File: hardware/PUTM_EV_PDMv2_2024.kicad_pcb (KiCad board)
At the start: 4 copper layers, 58 x 87.3 mm, 159 parts, among them IC1 BTS722204ESAXUMA1, IC2 BTS722204ESAXUMA1, IC3 BTS722204ESAXUMA1, IC4 BTS722204ESAXUMA1, J1 74650073R, J4 Conn_01x06, J5 UMPT-08-01-L-RA-WT-P-TR, J6 FTSH-107-01-L-DV-K-A, J7 USB_C_Receptacle_USB2.0_14P, J8 UMPT-08-01-L-RA-WT-P-TR, U1 STM32G0C1KCTxN, U2 LD1117S33TR_SOT223, U3 LM2675M-5.0/NOPB, U4 MCP2542FDxMF

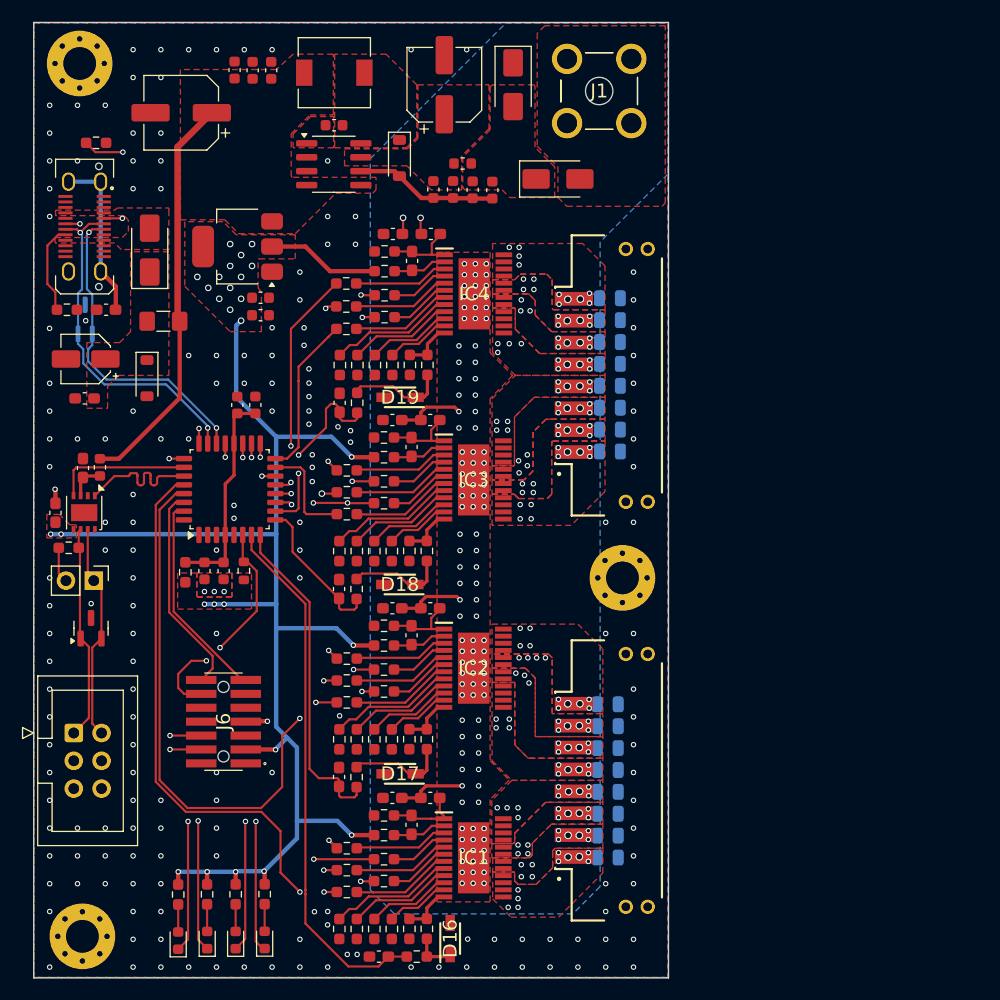
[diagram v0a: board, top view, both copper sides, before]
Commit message: cube->cmake port, current calc fix, spi datalength fix, hard-v1.1.0 sync
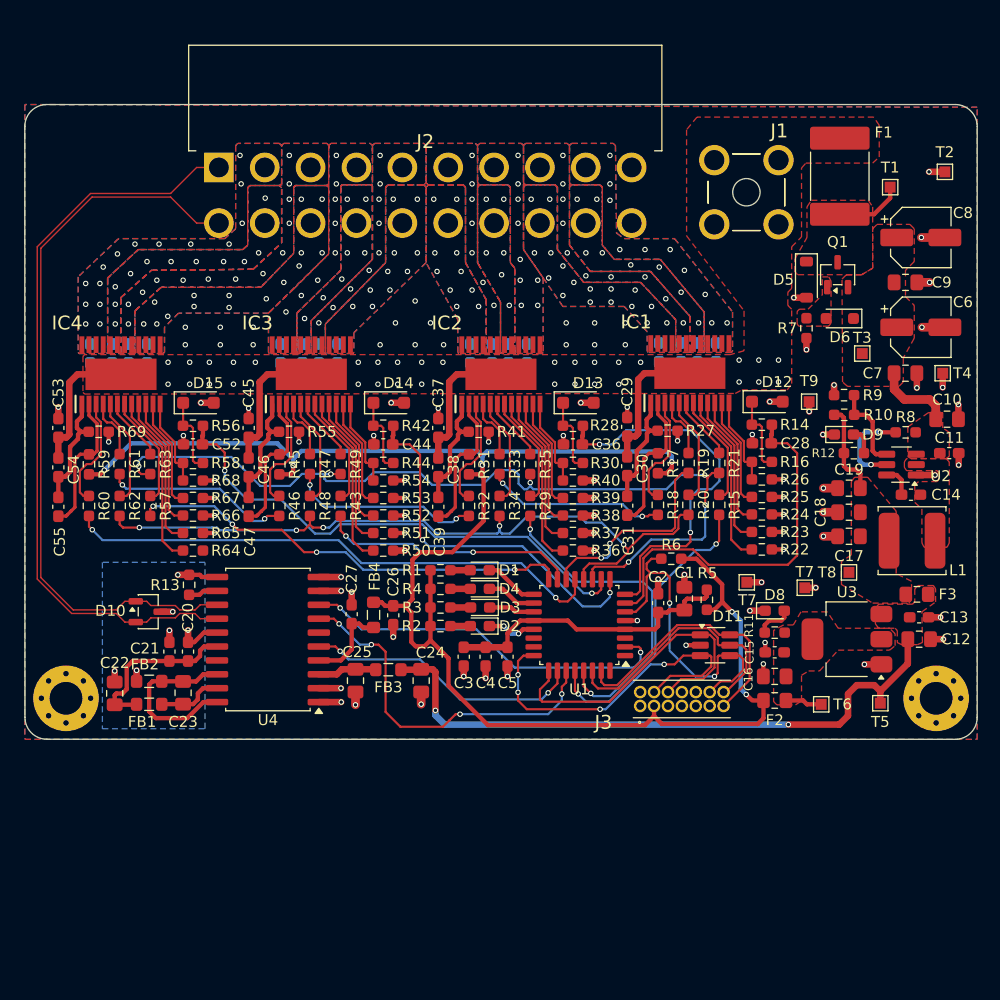
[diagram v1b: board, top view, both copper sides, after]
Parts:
- removed D16, D17, D18, D19: SKL34, SKL34:SODFL3718X140N
- removed G*** (x2): LOGO, LOGO
- removed G***: LOGO, Logos:SignatureBox25mm
- removed G***: LOGO, logos:PUTM_LOGO_15mm
- removed J4: Conn_01x06, Connector_IDC:IDC-Header_2x03_P2.54mm_Vertical
- removed J5, J8: UMPT-08-01-L-RA-WT-P-TR, UMPT-08-01-L-RA-WT-P-TR:SAMTEC_UMPT-08-01-L-RA-WT-P-TR
- removed J6: FTSH-107-01-L-DV-K-A, FTSH-107-01-L-DV-K-A:FTSH-107-XX-YYY-DV-K-A
- removed J7: USB_C_Receptacle_USB2.0_14P, Connector_USB:USB_C_Receptacle_JAE_DX07S024WJ3R400
- removed JP1: Jumper_2_Bridged, Connector_PinHeader_2.54mm:PinHeader_1x02_P2.54mm_Vertical
- removed L2: 47u, Inductor_SMD:L_6.3x6.3_H3
- removed the REF** at (174.6, 105.2)
- removed the REF** at (125.0, 58.2)
- removed the REF** at (125.2, 138.0)
- added C54: 22n, Capacitor_SMD:C_0603_1608Metric_Pad1.08x0.95mm_HandSolder, F.Cu at (123.0, 95.2)
- added C55: 470n, Capacitor_SMD:C_0603_1608Metric_Pad1.08x0.95mm_HandSolder, F.Cu at (123.0, 98.8)
- added C56: 10n, Capacitor_SMD:C_0603_1608Metric_Pad1.08x0.95mm_HandSolder, B.Cu at (126.0, 84.8)
- added C57: 10n, Capacitor_SMD:C_0603_1608Metric_Pad1.08x0.95mm_HandSolder, B.Cu at (128.0, 84.8)
- added C58: 10n, Capacitor_SMD:C_0603_1608Metric_Pad1.08x0.95mm_HandSolder, B.Cu at (129.5, 84.8)
- added C59: 10n, Capacitor_SMD:C_0603_1608Metric_Pad1.08x0.95mm_HandSolder, B.Cu at (131.2, 84.8)
- added D13: 40V/3A, Diode_SMD:D_SOD-123F, F.Cu at (170.6, 89.2)
- added D14: 40V/3A, Diode_SMD:D_SOD-123F, F.Cu at (153.2, 89.2)
- added D15: 40V/3A, Diode_SMD:D_SOD-123F, F.Cu at (135.8, 89.2)
- added F2: 6V/1A, Fuse:Fuse_0805_2012Metric_Pad1.15x1.40mm_HandSolder, F.Cu at (188.5, 116.5)
- added F3: 6V/1A, Fuse:Fuse_0805_2012Metric_Pad1.15x1.40mm_HandSolder, F.Cu at (201.5, 106.8)
- added FB1: 2K@100MHz, Inductor_SMD:L_0805_2012Metric_Pad1.05x1.20mm_HandSolder, F.Cu at (131.3, 116.8)
- added FB3: 2K@100MHz, Inductor_SMD:L_0805_2012Metric_Pad1.05x1.20mm_HandSolder, F.Cu at (153.2, 113.6)
- added FB4: 2K@100MHz, Inductor_SMD:L_0805_2012Metric_Pad1.05x1.20mm_HandSolder, F.Cu at (151.8, 108.6)
- added J2: IPBS-110-01-XX-D-GP, PDM:IPBT110H1TDRAGP, F.Cu at (137.7, 67.8)
- added J3: FTSH-107-01-L-D-K, PDM:FTSH-107-XX-YYY-D-K, F.Cu at (176.2, 117.0)
- added Q1: 30V/5A, Package_TO_SOT_SMD:SOT-23-3, F.Cu at (194.2, 77.5)
- added R66: 10k, Resistor_SMD:R_0603_1608Metric_Pad0.98x0.95mm_HandSolder, F.Cu at (135.3, 99.5)
- added R67: 10k, Resistor_SMD:R_0603_1608Metric_Pad0.98x0.95mm_HandSolder, F.Cu at (135.3, 98.0)
- added R68: 1k2, Resistor_SMD:R_0603_1608Metric_Pad0.98x0.95mm_HandSolder, F.Cu at (135.3, 96.3)
- added R69: 47R, Resistor_SMD:R_0603_1608Metric_Pad0.98x0.95mm_HandSolder, F.Cu at (126.7, 91.9)
- added REF**: MountingHole_3mm_Pad_Via, MountingHole:MountingHole_3mm_Pad_Via, F.Cu at (123.8, 116.2)
- added REF**: MountingHole_3mm_Pad_Via, MountingHole:MountingHole_3mm_Pad_Via, F.Cu at (203.2, 116.2)
- added T1: TP_VCC, TestPoint:TestPoint_Pad_1.0x1.0mm, F.Cu at (199.1, 69.5)
- added T2: TP_GND, TestPoint:TestPoint_Pad_1.0x1.0mm, F.Cu at (204.1, 68.2)
- added T3: TP_VCC, TestPoint:TestPoint_Pad_1.0x1.0mm, F.Cu at (196.5, 84.8)
- added T4: TP_GND, TestPoint:TestPoint_Pad_1.0x1.0mm, F.Cu at (203.8, 86.5)
- added T5: TP_+5V, TestPoint:TestPoint_Pad_1.0x1.0mm, F.Cu at (198.2, 116.7)
- added T6: TP_+3V3, TestPoint:TestPoint_Pad_1.0x1.0mm, F.Cu at (192.8, 116.8)
- added T7: TP_GND, TestPoint:TestPoint_Pad_1.0x1.0mm, F.Cu at (191.2, 106.2)
- added T7: TP_GND, TestPoint:TestPoint_Pad_1.0x1.0mm, F.Cu at (185.9, 105.7)
- added T8: TP_+5V, TestPoint:TestPoint_Pad_1.0x1.0mm, F.Cu at (195.3, 104.7)
- added T9: TP_GND, TestPoint:TestPoint_Pad_1.0x1.0mm, F.Cu at (191.7, 89.2)
- C1, C7: value 100n -> 10u; footprint Capacitor_SMD:C_0603_1608Metric -> Capacitor_SMD:C_0805_2012Metric_Pad1.18x1.45mm_HandSolder
- C10, C16: value 100n -> 22u; footprint Capacitor_SMD:C_0603_1608Metric -> Capacitor_SMD:C_0805_2012Metric_Pad1.18x1.45mm_HandSolder
- C11, C15, C5: value 1u -> 100n; footprint Capacitor_SMD:C_0603_1608Metric -> Capacitor_SMD:C_0603_1608Metric_Pad1.08x0.95mm_HandSolder
- C12: value 10n -> 10u; footprint Capacitor_SMD:C_0603_1608Metric -> Capacitor_SMD:C_0805_2012Metric_Pad1.18x1.45mm_HandSolder
- C13: footprint Capacitor_SMD:C_0603_1608Metric -> Capacitor_SMD:C_0603_1608Metric_Pad1.08x0.95mm_HandSolder
- C14: value 68u -> 100n; footprint Capacitor_SMD:CP_Elec_6.3x5.4 -> Capacitor_SMD:C_0603_1608Metric_Pad1.08x0.95mm_HandSolder
- C17: value 220p -> 22u; footprint Capacitor_SMD:C_0603_1608Metric_Pad1.08x0.95mm_HandSolder -> Capacitor_SMD:C_0805_2012Metric_Pad1.18x1.45mm_HandSolder
- C18: value 100n -> 22u; footprint Capacitor_SMD:C_0603_1608Metric_Pad1.08x0.95mm_HandSolder -> Capacitor_SMD:C_0805_2012Metric_Pad1.18x1.45mm_HandSolder
- C19: value 22n -> 22u; footprint Capacitor_SMD:C_0603_1608Metric_Pad1.08x0.95mm_HandSolder -> Capacitor_SMD:C_0805_2012Metric_Pad1.18x1.45mm_HandSolder
- C2: value 4.7u -> 4u7; footprint Capacitor_SMD:C_0603_1608Metric -> Capacitor_SMD:C_0603_1608Metric_Pad1.08x0.95mm_HandSolder
- C20: value 470n -> 100n
- C21: footprint Capacitor_SMD:C_0805_2012Metric -> Capacitor_SMD:C_0603_1608Metric_Pad1.08x0.95mm_HandSolder; moved to F.Cu
- C22, C23, C24: value 10n -> 47u; footprint Capacitor_SMD:C_0805_2012Metric -> Capacitor_SMD:C_0805_2012Metric_Pad1.18x1.45mm_HandSolder; moved to F.Cu
- C25: value 100n -> 47u; footprint Capacitor_SMD:C_0603_1608Metric_Pad1.08x0.95mm_HandSolder -> Capacitor_SMD:C_0805_2012Metric_Pad1.18x1.45mm_HandSolder
- C27: value 22u -> 10n; footprint Capacitor_SMD:CP_Elec_4x4.5 -> Capacitor_SMD:C_0603_1608Metric_Pad1.08x0.95mm_HandSolder
- C28: value 1u -> 220p
- C29, C37, C45: value 220p -> 100n
- C3: value 100n -> 4u7; footprint Capacitor_SMD:C_0603_1608Metric -> Capacitor_SMD:C_0603_1608Metric_Pad1.08x0.95mm_HandSolder
- C30, C38, C46: value 100n -> 22n
- C31, C39, C47: value 22n -> 470n
- C32, C40, C48: value 470n -> 10n; moved to B.Cu
- C33, C34, C35, C41, C42, C43, C49, C50, C51: footprint Capacitor_SMD:C_0805_2012Metric -> Capacitor_SMD:C_0603_1608Metric_Pad1.08x0.95mm_HandSolder
- C36, C44, C52: value 10n -> 220p; footprint Capacitor_SMD:C_0805_2012Metric -> Capacitor_SMD:C_0603_1608Metric_Pad1.08x0.95mm_HandSolder; moved to F.Cu
- C4: value 4.7u -> 100n; footprint Capacitor_SMD:C_0603_1608Metric -> Capacitor_SMD:C_0603_1608Metric_Pad1.08x0.95mm_HandSolder
- C53: value 10n -> 100n
- C6: value 10u -> 22u; footprint Capacitor_SMD:C_0603_1608Metric -> Capacitor_SMD:CP_Elec_5x5.8
- C8: value 100n -> 22u; footprint Capacitor_SMD:C_0603_1608Metric -> Capacitor_SMD:CP_Elec_5x5.8
- C9: value 100u -> 10u; footprint Capacitor_SMD:CP_Elec_6.3x7.7 -> Capacitor_SMD:C_0805_2012Metric_Pad1.18x1.45mm_HandSolder
- D1, D2, D3, D4: value 150060SS75000 -> LED_Debug; footprint LED_SMD:LED_0603_1608Metric -> LED_SMD:LED_0603_1608Metric_Pad1.05x0.95mm_HandSolder
- D10: value 0.1/1A -> PESD5V0L2BT,215; footprint Diode_SMD:D_SMA -> Package_TO_SOT_SMD:SOT-23-3
- D11: value 6V -> SP0505BAHTG; footprint Diode_SMD:D_SOD-123 -> Package_TO_SOT_SMD:SOT-23-6_Handsoldering
- D12: value TPD2E2U06QDCKRQ1 -> 40V/3A; footprint Package_TO_SOT_SMD:SOT-323_SC-70_Handsoldering -> Diode_SMD:D_SOD-123F; moved to F.Cu
- D5: value SMAJ24CA-13-F -> 30V/200W; footprint Diode_SMD:D_SMA -> Diode_SMD:D_SOD-123
- D6: value SS26FL -> 9V1/200mW; footprint Diode_SMD:D_SOD-123 -> Diode_SMD:D_SOD-323_HandSoldering
- D8: value SS34ALH -> LED_+3V3; footprint Diode_SMD:D_SMA -> LED_SMD:LED_0603_1608Metric_Pad1.05x0.95mm_HandSolder
- D9: value PESD2CAN.215 -> LED_+5V; footprint Package_TO_SOT_SMD:SOT-23 -> LED_SMD:LED_0603_1608Metric_Pad1.05x0.95mm_HandSolder
- F1: value 5V/0.5A -> 33V/1A5; footprint Fuse:Fuse_1206_3216Metric_Pad1.42x1.75mm_HandSolder -> Fuse:Fuse_2920_7451Metric_Pad2.10x5.45mm_HandSolder
- FB2: value 60R@100MHz -> 2K@100MHz; footprint Inductor_SMD:L_0603_1608Metric -> Inductor_SMD:L_0805_2012Metric_Pad1.05x1.20mm_HandSolder
- IC1, IC2, IC3, IC4: footprint BTS722204ESAXUMA1:SOP65P600X115-25N -> PDM:SOP65P600X115-25N
- J1: footprint Redcube conn:74650073R -> PDM:74650073R
- L1: value 300n -> 68u/1A4; footprint Inductor_SMD:L_0603_1608Metric -> Inductor_SMD:L_TDK_VLS6045EX_VLS6045AF
- R1, R2, R3, R4: value 150 -> 150R
- R10: value 10k -> 100k
- R11, R12: value 10k -> 1k
- R13: value 1.2k -> 100k
- R14: value 47 -> 4k7
- R15, R16: value 330 -> 4k7
- R17: value 330 -> 470R
- R18, R34, R35, R48, R49, R62, R63: value 330 -> 330R
- R19: value 100k -> 330R; footprint Resistor_SMD:R_0603_1608Metric -> Resistor_SMD:R_0603_1608Metric_Pad0.98x0.95mm_HandSolder
- R20: value 0 -> 330R
- R21: value 120 -> 330R
- R22, R23: value 5.1k -> 10k
- R24, R25, R38, R39, R52, R53: value 4.7k -> 10k
- R26, R40, R54: value 470 -> 1k2
- R27, R41, R55: value 4.7k -> 47R
- R28, R29, R30, R42, R43, R44, R56, R57, R58: value 10k -> 4k7
- R31, R45, R59: value 10k -> 470R
- R32, R46, R60: value 1.2k -> 330R
- R33, R47, R61: value 47 -> 330R
- R36, R37, R50, R51, R64, R65: value 330 -> 10k
- R5: value 4.7k -> 0
- R6: value 4.7k -> 100k
- R7: value 470 -> 100k
- R8: value 4.7k -> 510k
- R9: value 10k -> 13k3
- U2: value LD1117S33TR_SOT223 -> TPS54202HDDCR; footprint Package_TO_SOT_SMD:SOT-223-3_TabPin2 -> Package_TO_SOT_SMD:SOT-23-6_Handsoldering
- U3: value LM2675M-5.0/NOPB -> LM1117-3.3; footprint Package_SO:SOIC-8_3.9x4.9mm_P1.27mm -> Package_TO_SOT_SMD:SOT-223-3_TabPin2
- U4: value MCP2542FDxMF -> ADM3057ExRW; footprint Package_DFN_QFN:DFN-8-1EP_3x3mm_P0.65mm_EP1.55x2.4mm -> Package_SO:SOIC-20W_7.5x12.8mm_P1.27mm
- moved C14 75.3 mm to (200.9, 97.7), turned to 0 degrees
- moved C16 74.2 mm to (188.5, 114.2), turned to 180 degrees
- moved R22 71.3 mm to (187.3, 102.6)
- moved C12 71.2 mm to (201.7, 110.8)
- moved D9 71.0 mm to (194.8, 92.2), turned to 0 degrees
- moved C10 71.0 mm to (204.2, 90.8), turned to 0 degrees
- moved C15 70.3 mm to (188.5, 112.0), turned to 180 degrees
- moved R9 67.1 mm to (194.8, 88.5), turned to 0 degrees
- moved R23 66.7 mm to (187.3, 101.0)
- moved C13 66.2 mm to (201.7, 108.8)
- moved R10 64.7 mm to (194.8, 90.3), turned to 180 degrees
- moved C11 64.5 mm to (204.4, 93.8), turned to 180 degrees
- moved U3 63.9 mm to (195.1, 110.8), turned to 180 degrees
- moved U2 63.9 mm to (200.1, 94.9)
- moved F1 63.2 mm to (194.4, 68.5), turned to 90 degrees
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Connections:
- C1 pad 1: /STM_VCC -> /MCU/STM_VCC
- C10 pad 1: +5V -> +24V
- C11 pad 1: +3.3V -> GND
- C11 pad 2: GND -> +24V
- C12 pad 1: /Power/CB -> +5V
- C12 pad 2: /Power/SW_L -> GND
- C13 pad 1: +3.3V -> +5V
- C14 pad 1: +5V -> /Power/BOOT_+5V
- C14 pad 2: GND -> /Power/SW_+5V
- C15 pad 1: +5V -> /Power/VO_+3.3V
- C16 pad 1: +5V -> /Power/VO_+3.3V
- C17 pad 1: /FUSE1_IS -> /Power/+5V_OUT
- C18 pad 1: +BATT -> /Power/+5V_OUT
- C19 pad 1: +BATT -> /Power/+5V_OUT
- C19 pad 2: Net-(IC1-GND_1) -> GND
- C2 pad 1: /STM_VCC -> /MCU/STM_VCC
- C20 pad 1: Net-(IC1-GND_1) -> /CAN/CAN_GND_ISO
- C20 pad 2: Net-(IC1-VDD) -> /CAN/VISOIN
- C21 pad 1: OUT1_0 -> /CAN/VISOIN
- C21 pad 2: GND -> /CAN/CAN_GND_ISO
- C22 pad 1: OUT1_1 -> /CAN/CAN_GND_ISO
- C22 pad 2: GND -> /CAN/VISOIN
- C23 pad 1: OUT1_2 -> /CAN/GNDISO
- C23 pad 2: GND -> /CAN/VISOOUT
- C24 pad 1: OUT1_3 -> GND
- C24 pad 2: GND -> +5V
- C25 pad 1: +3.3V -> /CAN/VCC
- C26 pad 1: Net-(U4-VDD) -> +3V3
- C27 pad 1: Net-(D10-K) -> /CAN/VIO
- C28 pad 1: Net-(D10-K) -> /MCU/FUSE_IS0
- C29 pad 1: /FUSE2_IS -> +BATT
- C3 pad 1: /STM_VCC -> /MCU/STM_VCC
- C30 pad 2: GND -> /Power controllers/IC_0/PC0_GND
- C31 pad 1: +BATT -> /Power controllers/IC_0/PC0_GND
- C31 pad 2: Net-(IC2-GND_1) -> /Power controllers/IC_0/VDD
- C32 pad 1: Net-(IC2-GND_1) -> OUT0_0
- C32 pad 2: Net-(IC2-VDD) -> GND
- C33 pad 1: OUT2_0 -> OUT0_1
- C34 pad 1: OUT2_1 -> OUT0_2
- C35 pad 1: OUT2_2 -> OUT0_3
- C36 pad 1: OUT2_3 -> /MCU/FUSE_IS1
- C37 pad 1: /FUSE3_IS -> +BATT
- C38 pad 2: GND -> /Power controllers/IC_1/PC1_GND
- C39 pad 1: +BATT -> /Power controllers/IC_1/PC1_GND
- C39 pad 2: Net-(IC3-GND_1) -> /Power controllers/IC_1/VDD
- C4 pad 1: /STM_VCC -> /MCU/STM_VCC
- C40 pad 1: Net-(IC3-GND_1) -> OUT1_0
- C40 pad 2: Net-(IC3-VDD) -> GND
- C41 pad 1: OUT3_0 -> OUT1_1
- C42 pad 1: OUT3_1 -> OUT1_2
- C43 pad 1: OUT3_2 -> OUT1_3
- C44 pad 1: OUT3_3 -> /MCU/FUSE_IS2
- C45 pad 1: /FUSE4_IS -> +BATT
- C46 pad 2: GND -> /Power controllers/IC_2/PC2_GND
- C47 pad 1: +BATT -> /Power controllers/IC_2/PC2_GND
- C47 pad 2: Net-(IC4-GND_1) -> /Power controllers/IC_2/VDD
- C48 pad 1: Net-(IC4-GND_1) -> OUT2_0
- C48 pad 2: Net-(IC4-VDD) -> GND
- C49 pad 1: OUT4_0 -> OUT2_1
- C5 pad 1: GND -> /MCU/STM_VCC
- C5 pad 2: /Power/VIN_L -> GND
- C50 pad 1: OUT4_1 -> OUT2_2
- C51 pad 1: OUT4_2 -> OUT2_3
- C52 pad 1: OUT4_3 -> /MCU/FUSE_IS3
- C53 pad 1: Net-(J7-SHIELD) -> +BATT
- C6 pad 1: GND -> +24V
- C6 pad 2: /Power/VIN_L -> GND
- C7 pad 1: GND -> +24V
- C7 pad 2: /Power/VIN_SW_REG -> GND
- C8 pad 1: GND -> +24V
- C8 pad 2: /Power/VIN_SW_REG -> GND
- C9 pad 1: /Power/VIN_SW_REG -> +24V
- D1 pad 1: /LED1 -> /MCU/LED3
- D1 pad 2: Net-(D1-A) -> /MCU/LD_3_R
- D10 pad 1: Net-(D10-K) -> /CAN/CAN.N
- D10 pad 2: VBUS -> /CAN/CAN.P
- D11 pad 1: Net-(D10-K) -> /Connectors/SW.CLK
- D12 pad 1: /D- -> /Power controllers/IC_0/R_IS_PROT
- D12 pad 2: /D+ -> GND
- D2 pad 1: /LED2 -> /MCU/LED2
- D2 pad 2: Net-(D2-A) -> /MCU/LD_2_R
- D3 pad 1: /LED3 -> /MCU/LED1
- D3 pad 2: Net-(D3-A) -> /MCU/LD_1_R
- D4 pad 1: /LED4 -> /MCU/LED0
- D4 pad 2: Net-(D4-A) -> /MCU/LD_0_R
- D5 pad 1: GND -> /Power/RPP_D
- D5 pad 2: /Power/VIN_L -> GND
- D6 pad 1: /Power/SW_L -> +24V
- D6 pad 2: GND -> /Power/RPP_G
- D8 pad 1: /Power/VIN_L -> GND
- D8 pad 2: +BATT -> /Power/D3V3_R1k
- D9 pad 1: CAN_L -> GND
- D9 pad 2: CAN_H -> /Power/D5V_R1k
- F1 pad 1: +5V -> /Power/RPP_D
- F1 pad 2: Net-(D10-K) -> +BATT
- FB2 pad 1: +5V -> /CAN/GNDISO
- FB2 pad 2: Net-(U4-VDD) -> /CAN/CAN_GND_ISO
- IC1 pad 1: Net-(IC1-GND_1) -> /Power controllers/IC_0/PC0_GND
- IC1 pad 10: /Controllers/IC_1/IN2 -> /Power controllers/IC_0/IN2
- IC1 pad 11: /Controllers/IC_1/IN3 -> /Power controllers/IC_0/IN3
- IC1 pad 12: Net-(IC1-IS) -> /Power controllers/IC_0/IS
- IC1 pad 13: OUT1_3 -> OUT0_3
- IC1 pad 14: OUT1_3 -> OUT0_3
- IC1 pad 15: OUT1_3 -> OUT0_3
- IC1 pad 16: OUT1_3 -> OUT0_3
- IC1 pad 17: OUT1_2 -> OUT0_2
- IC1 pad 18: OUT1_2 -> OUT0_2
- IC1 pad 19: OUT1_1 -> OUT0_1
- IC1 pad 2: Net-(IC1-VDD) -> /Power controllers/IC_0/VDD
- IC1 pad 20: OUT1_1 -> OUT0_1
- IC1 pad 21: OUT1_0 -> OUT0_0
- IC1 pad 22: OUT1_0 -> OUT0_0
- IC1 pad 23: OUT1_0 -> OUT0_0
- IC1 pad 24: OUT1_0 -> OUT0_0
- IC1 pad 3: Net-(IC1-SO) -> /Power controllers/IC_0/SO
- IC1 pad 4: Net-(IC1-SI) -> /Power controllers/IC_0/SI
- IC1 pad 5: Net-(IC1-SCLK) -> /Power controllers/IC_0/SCLK
- IC1 pad 6: Net-(IC1-CSN) -> /Power controllers/IC_0/CSN
- IC1 pad 7: Net-(IC1-LHI) -> /Power controllers/IC_0/LHI
- IC1 pad 8: /Controllers/IC_1/IN0 -> /Power controllers/IC_0/IN0
- IC1 pad 9: /Controllers/IC_1/IN1 -> /Power controllers/IC_0/IN1
- IC2 pad 1: Net-(IC2-GND_1) -> /Power controllers/IC_1/PC1_GND
- IC2 pad 10: /Controllers/IC_2/IN2 -> /Power controllers/IC_1/IN2
- IC2 pad 11: /Controllers/IC_2/IN3 -> /Power controllers/IC_1/IN3
- IC2 pad 12: Net-(IC2-IS) -> /Power controllers/IC_1/IS
- IC2 pad 13: OUT2_3 -> OUT1_3
- IC2 pad 14: OUT2_3 -> OUT1_3
- IC2 pad 15: OUT2_3 -> OUT1_3
- IC2 pad 16: OUT2_3 -> OUT1_3
- IC2 pad 17: OUT2_2 -> OUT1_2
- IC2 pad 18: OUT2_2 -> OUT1_2
- IC2 pad 19: OUT2_1 -> OUT1_1
- IC2 pad 2: Net-(IC2-VDD) -> /Power controllers/IC_1/VDD
- IC2 pad 20: OUT2_1 -> OUT1_1
- IC2 pad 21: OUT2_0 -> OUT1_0
- IC2 pad 22: OUT2_0 -> OUT1_0
- IC2 pad 23: OUT2_0 -> OUT1_0
- IC2 pad 24: OUT2_0 -> OUT1_0
- IC2 pad 3: Net-(IC2-SO) -> /Power controllers/IC_1/SO
- IC2 pad 4: Net-(IC2-SI) -> /Power controllers/IC_1/SI
- IC2 pad 5: Net-(IC2-SCLK) -> /Power controllers/IC_1/SCLK
- IC2 pad 6: Net-(IC2-CSN) -> /Power controllers/IC_1/CSN
- IC2 pad 7: Net-(IC2-LHI) -> /Power controllers/IC_1/LHI
- IC2 pad 8: /Controllers/IC_2/IN0 -> /Power controllers/IC_1/IN0
- IC2 pad 9: /Controllers/IC_2/IN1 -> /Power controllers/IC_1/IN1
- IC3 pad 1: Net-(IC3-GND_1) -> /Power controllers/IC_2/PC2_GND
- IC3 pad 10: /Controllers/IC_3/IN2 -> /Power controllers/IC_2/IN2
- IC3 pad 11: /Controllers/IC_3/IN3 -> /Power controllers/IC_2/IN3
- IC3 pad 12: Net-(IC3-IS) -> /Power controllers/IC_2/IS
- IC3 pad 13: OUT3_3 -> OUT2_3
- IC3 pad 14: OUT3_3 -> OUT2_3
- IC3 pad 15: OUT3_3 -> OUT2_3
- IC3 pad 16: OUT3_3 -> OUT2_3
- IC3 pad 17: OUT3_2 -> OUT2_2
- IC3 pad 18: OUT3_2 -> OUT2_2
- IC3 pad 19: OUT3_1 -> OUT2_1
- IC3 pad 2: Net-(IC3-VDD) -> /Power controllers/IC_2/VDD
- IC3 pad 20: OUT3_1 -> OUT2_1
- IC3 pad 21: OUT3_0 -> OUT2_0
- IC3 pad 22: OUT3_0 -> OUT2_0
- IC3 pad 23: OUT3_0 -> OUT2_0
- IC3 pad 24: OUT3_0 -> OUT2_0
- IC3 pad 3: Net-(IC3-SO) -> /Power controllers/IC_2/SO
- IC3 pad 4: Net-(IC3-SI) -> /Power controllers/IC_2/SI
- IC3 pad 5: Net-(IC3-SCLK) -> /Power controllers/IC_2/SCLK
- IC3 pad 6: Net-(IC3-CSN) -> /Power controllers/IC_2/CSN
- IC3 pad 7: Net-(IC3-LHI) -> /Power controllers/IC_2/LHI
- IC3 pad 8: /Controllers/IC_3/IN0 -> /Power controllers/IC_2/IN0
- IC3 pad 9: /Controllers/IC_3/IN1 -> /Power controllers/IC_2/IN1
- IC4 pad 1: Net-(IC4-GND_1) -> /Power controllers/IC_3/PC3_GND
- IC4 pad 10: /Controllers/IC_4/IN2 -> /Power controllers/IC_3/IN2
- IC4 pad 11: /Controllers/IC_4/IN3 -> /Power controllers/IC_3/IN3
- IC4 pad 12: Net-(IC4-IS) -> /Power controllers/IC_3/IS
- IC4 pad 13: OUT4_3 -> OUT3_3
- IC4 pad 14: OUT4_3 -> OUT3_3
- IC4 pad 15: OUT4_3 -> OUT3_3
- IC4 pad 16: OUT4_3 -> OUT3_3
- IC4 pad 17: OUT4_2 -> OUT3_2
- IC4 pad 18: OUT4_2 -> OUT3_2
- IC4 pad 19: OUT4_1 -> OUT3_1
- IC4 pad 2: Net-(IC4-VDD) -> /Power controllers/IC_3/VDD
- IC4 pad 20: OUT4_1 -> OUT3_1
- IC4 pad 21: OUT4_0 -> OUT3_0
- IC4 pad 22: OUT4_0 -> OUT3_0
- IC4 pad 23: OUT4_0 -> OUT3_0
- IC4 pad 24: OUT4_0 -> OUT3_0
- IC4 pad 3: Net-(IC4-SO) -> /Power controllers/IC_3/SO
- IC4 pad 4: Net-(IC4-SI) -> /Power controllers/IC_3/SI
- IC4 pad 5: Net-(IC4-SCLK) -> /Power controllers/IC_3/SCLK
- IC4 pad 6: Net-(IC4-CSN) -> /Power controllers/IC_3/CSN
- IC4 pad 7: Net-(IC4-LHI) -> /Power controllers/IC_3/LHI
- IC4 pad 8: /Controllers/IC_4/IN0 -> /Power controllers/IC_3/IN0
- IC4 pad 9: /Controllers/IC_4/IN1 -> /Power controllers/IC_3/IN1
- L1 pad 1: /Power/VIN_L -> /Power/SW_+5V
- L1 pad 2: /Power/VIN_SW_REG -> /Power/+5V_OUT
- R1 pad 1: +3.3V -> /MCU/LD_3_R
- R1 pad 2: Net-(D3-A) -> +3V3
- R10 pad 1: GND -> /Power/FB_+5V
- R10 pad 2: /Controllers/IC_1/IN1 -> /Power/+5V_OUT
- R11 pad 1: GND -> /Power/VO_+3.3V
- R11 pad 2: /Controllers/IC_1/IN2 -> /Power/D3V3_R1k
- R12 pad 1: GND -> /Power/+5V_OUT
- R12 pad 2: /Controllers/IC_1/IN3 -> /Power/D5V_R1k
- R13 pad 1: Net-(IC1-IS) -> /CAN/CAN_GND_ISO
- R13 pad 2: GND -> /CAN/RS
- R14 pad 1: GND -> /MCU/FUSE_IS0
- R14 pad 2: Net-(IC1-GND_1) -> /Power controllers/IC_0/R_IS_PROT
- R15 pad 1: /Controllers/MISO_1 -> /MCU/LHI0
- R15 pad 2: Net-(IC1-SO) -> /Power controllers/IC_0/LHI
- R16 pad 1: /SPI1_MOSI -> /Power controllers/IC_0/R_IS_PROT
- R16 pad 2: Net-(IC1-SI) -> /Power controllers/IC_0/IS
- R17 pad 1: /SPI1_SCK -> +3V3
- R17 pad 2: Net-(IC1-SCLK) -> /Power controllers/IC_0/VDD
- R18 pad 1: /SPI1_NSS -> /Power controllers/IC_0/MISO
- R18 pad 2: Net-(IC1-CSN) -> /Power controllers/IC_0/SO
- R19 pad 1: +3.3V -> /MCU/SPI.MOSI
- R19 pad 2: /NRST -> /Power controllers/IC_0/SI
- R2 pad 1: +3.3V -> /MCU/LD_2_R
- R2 pad 2: Net-(D2-A) -> +3V3
- R20 pad 1: +3.3V -> /MCU/SPI.SCK
- R20 pad 2: /STM_VCC -> /Power controllers/IC_0/SCLK
- R21 pad 1: Net-(JP1-B) -> /MCU/SPI.NSS
- R21 pad 2: CAN_L -> /Power controllers/IC_0/CSN
- R22 pad 2: Net-(J7-CC1) -> /Power controllers/IC_0/IN0
- R23 pad 2: Net-(J7-CC2) -> /Power controllers/IC_0/IN1
- R24 pad 1: /FUSE2_IS -> GND
- R24 pad 2: Net-(D17-K) -> /Power controllers/IC_0/IN2
- R25 pad 1: /LHI_2 -> GND
- R25 pad 2: Net-(IC2-LHI) -> /Power controllers/IC_0/IN3
- R26 pad 1: +3.3V -> /Power controllers/IC_0/IS
- R26 pad 2: Net-(IC2-VDD) -> GND
- R27 pad 1: Net-(D17-K) -> GND
- R27 pad 2: Net-(IC2-IS) -> /Power controllers/IC_0/PC0_GND
- R28 pad 1: GND -> /MCU/FUSE_IS1
- R28 pad 2: /Controllers/IC_2/IN0 -> /Power controllers/IC_1/R_IS_PROT
- R29 pad 1: GND -> /MCU/LHI1
- R29 pad 2: /Controllers/IC_2/IN1 -> /Power controllers/IC_1/LHI
- R3 pad 1: +3.3V -> /MCU/LD_1_R
- R3 pad 2: Net-(D1-A) -> +3V3
- R30 pad 1: GND -> /Power controllers/IC_1/R_IS_PROT
- R30 pad 2: /Controllers/IC_2/IN2 -> /Power controllers/IC_1/IS
- R31 pad 1: GND -> +3V3
- R31 pad 2: /Controllers/IC_2/IN3 -> /Power controllers/IC_1/VDD
- R32 pad 1: Net-(IC2-IS) -> /Power controllers/IC_1/MISO
- R32 pad 2: GND -> /Power controllers/IC_1/SO
- R33 pad 1: GND -> /Power controllers/IC_0/MISO
- R33 pad 2: Net-(IC2-GND_1) -> /Power controllers/IC_1/SI
- R34 pad 1: /Controllers/MISO_2 -> /MCU/SPI.SCK
- R34 pad 2: Net-(IC2-SO) -> /Power controllers/IC_1/SCLK
- R35 pad 1: /Controllers/MISO_1 -> /MCU/SPI.NSS
- R35 pad 2: Net-(IC2-SI) -> /Power controllers/IC_1/CSN
- R36 pad 1: /SPI1_SCK -> GND
- R36 pad 2: Net-(IC2-SCLK) -> /Power controllers/IC_1/IN0
- R37 pad 1: /SPI1_NSS -> GND
- R37 pad 2: Net-(IC2-CSN) -> /Power controllers/IC_1/IN1
- R38 pad 1: /FUSE3_IS -> GND
- R38 pad 2: Net-(D18-K) -> /Power controllers/IC_1/IN2
- R39 pad 1: /LHI_3 -> GND
- R39 pad 2: Net-(IC3-LHI) -> /Power controllers/IC_1/IN3
- R4 pad 1: +3.3V -> /MCU/LD_0_R
- R4 pad 2: Net-(D4-A) -> +3V3
- R40 pad 1: +3.3V -> /Power controllers/IC_1/IS
- R40 pad 2: Net-(IC3-VDD) -> GND
- R41 pad 1: Net-(D18-K) -> GND
- R41 pad 2: Net-(IC3-IS) -> /Power controllers/IC_1/PC1_GND
- R42 pad 1: GND -> /MCU/FUSE_IS2
- R42 pad 2: /Controllers/IC_3/IN0 -> /Power controllers/IC_2/R_IS_PROT
- R43 pad 1: GND -> /MCU/LHI2
- R43 pad 2: /Controllers/IC_3/IN1 -> /Power controllers/IC_2/LHI
- R44 pad 1: GND -> /Power controllers/IC_2/R_IS_PROT
- R44 pad 2: /Controllers/IC_3/IN2 -> /Power controllers/IC_2/IS
- R45 pad 1: GND -> +3V3
- R45 pad 2: /Controllers/IC_3/IN3 -> /Power controllers/IC_2/VDD
- R46 pad 1: Net-(IC3-IS) -> /Power controllers/IC_2/MISO
- R46 pad 2: GND -> /Power controllers/IC_2/SO
- R47 pad 1: GND -> /Power controllers/IC_1/MISO
- R47 pad 2: Net-(IC3-GND_1) -> /Power controllers/IC_2/SI
- R48 pad 1: /Controllers/MISO_3 -> /MCU/SPI.SCK
- R48 pad 2: Net-(IC3-SO) -> /Power controllers/IC_2/SCLK
- R49 pad 1: /Controllers/MISO_2 -> /MCU/SPI.NSS
- R49 pad 2: Net-(IC3-SI) -> /Power controllers/IC_2/CSN
- R5 pad 1: /FUSE1_IS -> +3V3
- R5 pad 2: Net-(D16-K) -> /MCU/STM_VCC
- R50 pad 1: /SPI1_SCK -> GND
- R50 pad 2: Net-(IC3-SCLK) -> /Power controllers/IC_2/IN0
- R51 pad 1: /SPI1_NSS -> GND
- R51 pad 2: Net-(IC3-CSN) -> /Power controllers/IC_2/IN1
- R52 pad 1: /FUSE4_IS -> GND
- R52 pad 2: Net-(D19-K) -> /Power controllers/IC_2/IN2
- R53 pad 1: /LHI_4 -> GND
- R53 pad 2: Net-(IC4-LHI) -> /Power controllers/IC_2/IN3
- R54 pad 1: +3.3V -> /Power controllers/IC_2/IS
- R54 pad 2: Net-(IC4-VDD) -> GND
- R55 pad 1: Net-(D19-K) -> GND
- R55 pad 2: Net-(IC4-IS) -> /Power controllers/IC_2/PC2_GND
- R56 pad 1: GND -> /MCU/FUSE_IS3
- R56 pad 2: /Controllers/IC_4/IN0 -> /Power controllers/IC_3/R_IS_PROT
- R57 pad 1: GND -> /MCU/LHI3
- R57 pad 2: /Controllers/IC_4/IN1 -> /Power controllers/IC_3/LHI
- R58 pad 1: GND -> /Power controllers/IC_3/R_IS_PROT
- R58 pad 2: /Controllers/IC_4/IN2 -> /Power controllers/IC_3/IS
- R59 pad 1: GND -> +3V3
- R59 pad 2: /Controllers/IC_4/IN3 -> /Power controllers/IC_3/VDD
- R6 pad 1: /LHI_1 -> +3V3
- R6 pad 2: Net-(IC1-LHI) -> /Connectors/RST
- R60 pad 1: Net-(IC4-IS) -> /MCU/SPI.MISO
- R60 pad 2: GND -> /Power controllers/IC_3/SO
- R61 pad 1: GND -> /Power controllers/IC_2/MISO
- R61 pad 2: Net-(IC4-GND_1) -> /Power controllers/IC_3/SI
- R62 pad 1: /SPI1_MISO -> /MCU/SPI.SCK
- R62 pad 2: Net-(IC4-SO) -> /Power controllers/IC_3/SCLK
- R63 pad 1: /Controllers/MISO_3 -> /MCU/SPI.NSS
- R63 pad 2: Net-(IC4-SI) -> /Power controllers/IC_3/CSN
- R64 pad 1: /SPI1_SCK -> GND
- R64 pad 2: Net-(IC4-SCLK) -> /Power controllers/IC_3/IN0
- R65 pad 1: /SPI1_NSS -> GND
- R65 pad 2: Net-(IC4-CSN) -> /Power controllers/IC_3/IN1
- R7 pad 1: +3.3V -> GND
- R7 pad 2: Net-(IC1-VDD) -> /Power/RPP_G
- R8 pad 1: Net-(D16-K) -> /Power/EN
- R8 pad 2: Net-(IC1-IS) -> +24V
- R9 pad 2: /Controllers/IC_1/IN0 -> /Power/FB_+5V
- U1 pad 10: /FUSE4_IS -> /MCU/FUSE_IS3
- U1 pad 11: /SPI1_NSS -> /MCU/SPI.NSS
- U1 pad 12: /SPI1_SCK -> /MCU/SPI.SCK
- U1 pad 13: /SPI1_MISO -> /MCU/SPI.MISO
- U1 pad 14: /SPI1_MOSI -> /MCU/SPI.MOSI
- U1 pad 15: /LHI_3 -> /MCU/LHI2
- U1 pad 16: /LHI_4 -> /MCU/LHI3
- U1 pad 17: /LED4 -> /MCU/LED3
- U1 pad 18: /LED3 -> /MCU/LED0
- U1 pad 19: /LED2 -> /MCU/LED1
- U1 pad 2: unconnected-(U1-PC14-Pad2) -> /CAN/STBY_CAN
- U1 pad 20: /STM_VCC -> /MCU/STM_VCC
- U1 pad 21: /LED1 -> /MCU/LED2
- U1 pad 22: /D- -> unconnected-(U1-PA11/PA9-Pad22)
- U1 pad 23: /D+ -> unconnected-(U1-PA12/PA10-Pad23)
- U1 pad 24: /SWDIO -> /Connectors/SW.DIO
- U1 pad 25: /SWCLK -> /Connectors/SW.CLK
- U1 pad 26: /CAN_RXD -> /CAN/CAN.RX
- U1 pad 27: /CAN_TXD -> /CAN/CAN.TX
- U1 pad 28: /LHI_1 -> /MCU/LHI0
- U1 pad 29: /LHI_2 -> /MCU/LHI1
- U1 pad 30: /USART1_TX -> /Connectors/USART.TX
- U1 pad 31: /USART1_RX -> /Connectors/USART.RX
- U1 pad 4: /STM_VCC -> /MCU/STM_VCC
- U1 pad 6: /NRST -> /Connectors/RST
- U1 pad 7: /FUSE1_IS -> /MCU/FUSE_IS0
- U1 pad 8: /FUSE2_IS -> /MCU/FUSE_IS1
- U1 pad 9: /FUSE3_IS -> /MCU/FUSE_IS2
- U2 pad 2: +3.3V -> /Power/SW_+5V
- U2 pad 3: +5V -> +24V
- U3 pad 1: /Power/CB -> GND
- U3 pad 2: unconnected-(U3-NC-Pad2) -> /Power/VO_+3.3V
- U3 pad 3: unconnected-(U3-NC-Pad3) -> +5V
- U4 pad 1: /CAN_TXD -> GND
- U4 pad 3: Net-(U4-VDD) -> /CAN/VCC
- U4 pad 4: /CAN_RXD -> /CAN/VIO
- U4 pad 5: +3.3V -> /CAN/CAN.RX
- U4 pad 6: CAN_L -> unconnected-(U4-SILENT-Pad6)
- U4 pad 7: CAN_H -> /CAN/CAN.TX
- U4 pad 8: GND -> /CAN/STBY_CAN
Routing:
- net +3V3: track 0.00 -> 153.2 mm, vias 0 -> 6
- net +3.3V: track 135.0 -> 0.00 mm, vias 27 -> 0
- net /MCU/SPI.NSS: track 0.00 -> 81.5 mm, vias 0 -> 6
- net GND: track 16.3 -> 88.1 mm, vias 180 -> 93
- net /CAN/CAN.P: track 0.00 -> 68.5 mm
- net /CAN/CAN.N: track 0.00 -> 67.4 mm
- net /MCU/SPI.SCK: track 0.00 -> 66.1 mm, vias 0 -> 5
- net /SPI1_NSS: track 65.4 -> 0.00 mm, vias 6 -> 0
- net /SPI1_SCK: track 60.7 -> 0.00 mm, vias 5 -> 0
- net /LHI_1: track 51.6 -> 0.00 mm, vias 2 -> 0
- net /LHI_2: track 51.5 -> 0.00 mm, vias 2 -> 0
- net /MCU/SPI.MISO: track 0.00 -> 49.8 mm, vias 0 -> 2
- net /FUSE1_IS: track 48.8 -> 0.00 mm
- net /LED1: track 48.3 -> 0.00 mm, vias 2 -> 0
- net /LED2: track 48.2 -> 0.00 mm, vias 2 -> 0
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- added copper zone on F.Cu, net +24V
- added copper zone on In1.Cu, net +BATT
- added copper zone on In2.Cu, net +BATT
- added copper zone on B.Cu, net /CAN/CAN_GND_ISO
- added copper zone on F.Cu, net /Power/+5V_OUT
- added copper zone on F.Cu, net /Power/RPP_D
- added copper zone on F.Cu, net /Power/RPP_G
- added copper zone on F.Cu, net /Power/SW_+5V
- added copper zone on F.Cu, net /Power/VO_+3.3V
- added copper zone on B.Cu, net OUT0_0
- added copper zone on F.Cu, net OUT0_0
- added copper zone on In1.Cu, net OUT0_0
- added copper zone on In2.Cu, net OUT0_0
- added copper zone on B.Cu, net OUT0_1
- added copper zone on F.Cu, net OUT0_1
- added copper zone on In1.Cu, net OUT0_1
- added copper zone on In2.Cu, net OUT0_1
- added copper zone on B.Cu, net OUT0_2
- added copper zone on F.Cu, net OUT0_2
- added copper zone on In1.Cu, net OUT0_2
- added copper zone on In2.Cu, net OUT0_2
- added copper zone on B.Cu, net OUT0_3
- added copper zone on F.Cu, net OUT0_3
- added copper zone on In1.Cu, net OUT0_3
- added copper zone on In2.Cu, net OUT0_3
- removed copper zone on F.Cu, net +3.3V
- removed copper zone on In1.Cu, net +3.3V
- removed copper zone on B.Cu, net +BATT
- removed copper zone on F.Cu, net /Power/CB
- removed copper zone on F.Cu, net /Power/SW_L
- removed copper zone on F.Cu, net /Power/VIN_L
- removed copper zone on F.Cu, net /Power/VIN_SW_REG
- removed copper zone on F.Cu, net Net-(D10-K)
- removed copper zone on B.Cu, net OUT4_0
- removed copper zone on F.Cu, net OUT4_0
- removed copper zone on In1.Cu, net OUT4_0
- removed copper zone on In2.Cu, net OUT4_0
- removed copper zone on B.Cu, net OUT4_1
- removed copper zone on F.Cu, net OUT4_1
- removed copper zone on In1.Cu, net OUT4_1
- removed copper zone on In2.Cu, net OUT4_1
- removed copper zone on B.Cu, net OUT4_2
- removed copper zone on F.Cu, net OUT4_2
- removed copper zone on In1.Cu, net OUT4_2
- removed copper zone on In2.Cu, net OUT4_2
- removed copper zone on B.Cu, net OUT4_3
- removed copper zone on F.Cu, net OUT4_3
- removed copper zone on In1.Cu, net OUT4_3
- removed copper zone on In2.Cu, net OUT4_3
- removed copper zone on F.Cu, net VBUS
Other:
- board size 58 x 87.3 mm -> 87 x 58 mm
- board text removed: "Kacper Biadała"
- board text removed: "v2.0"
